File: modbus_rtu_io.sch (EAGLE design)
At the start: 60 parts, among them IC1 MAX3485ESA, IC5 ATMEGA48/88/168-PU, K1 AQY27SMD, K2 AQY22SOP, K3 G6D-1A-ASI12VDC, K4 RP418005, K5 AQG12105, K7 G6D-1A-ASI12VDC, K8 AQY22SOP, T1 BC846, T2 BC846, T4 BC846

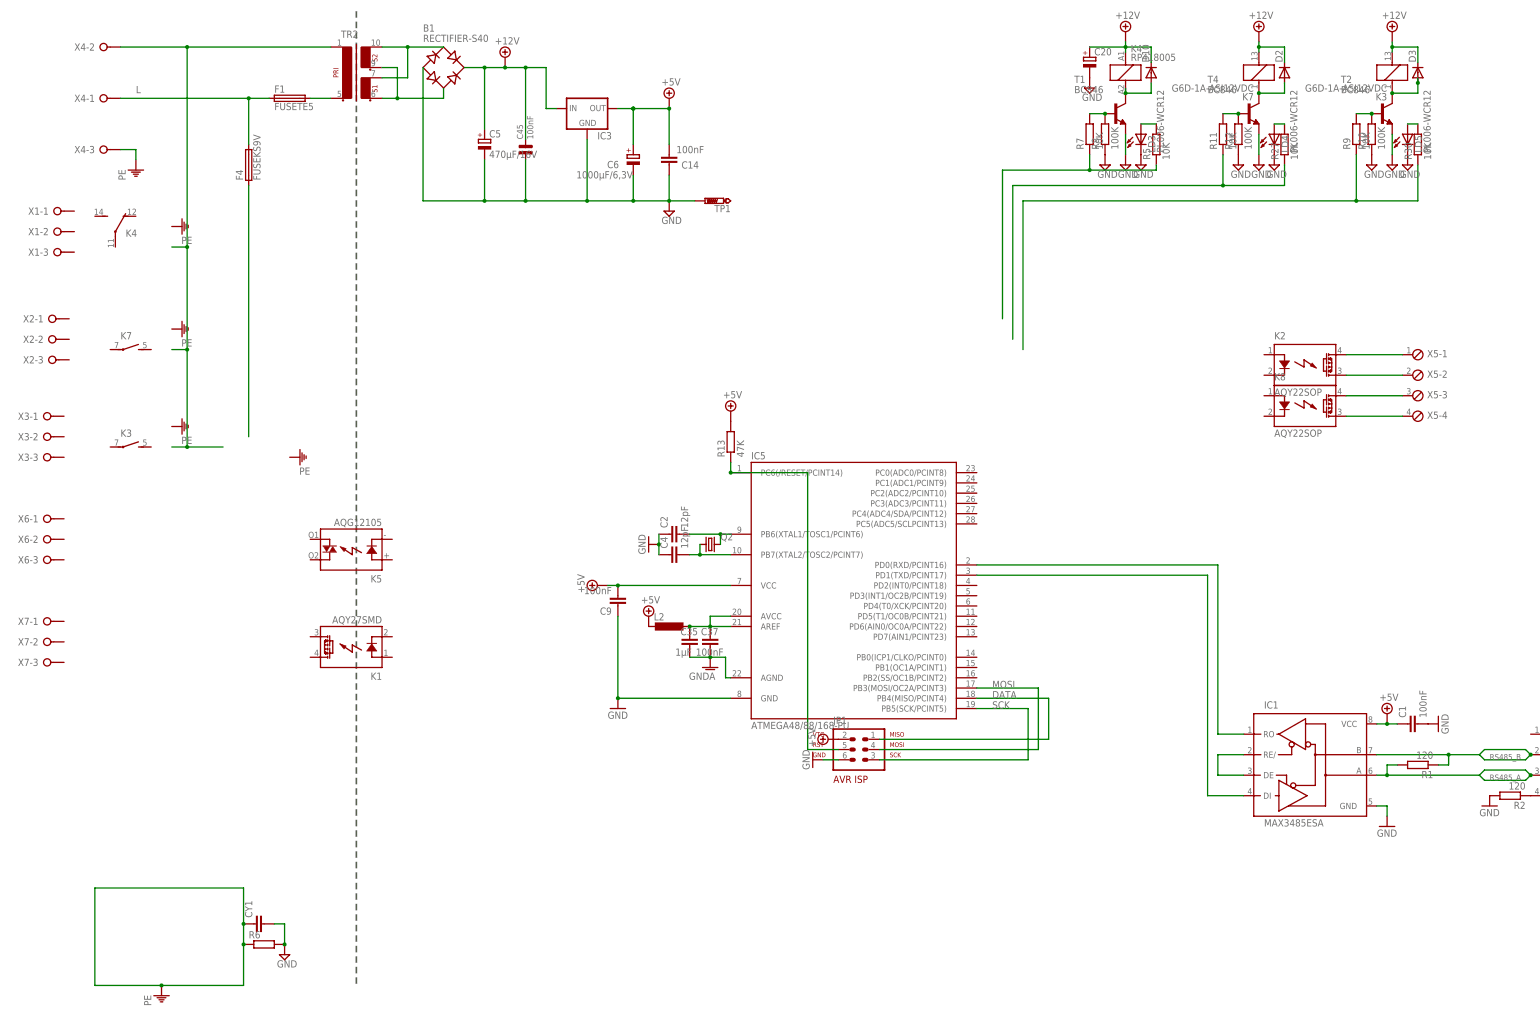
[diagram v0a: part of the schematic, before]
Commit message: Relais geändert, Routing angefangen
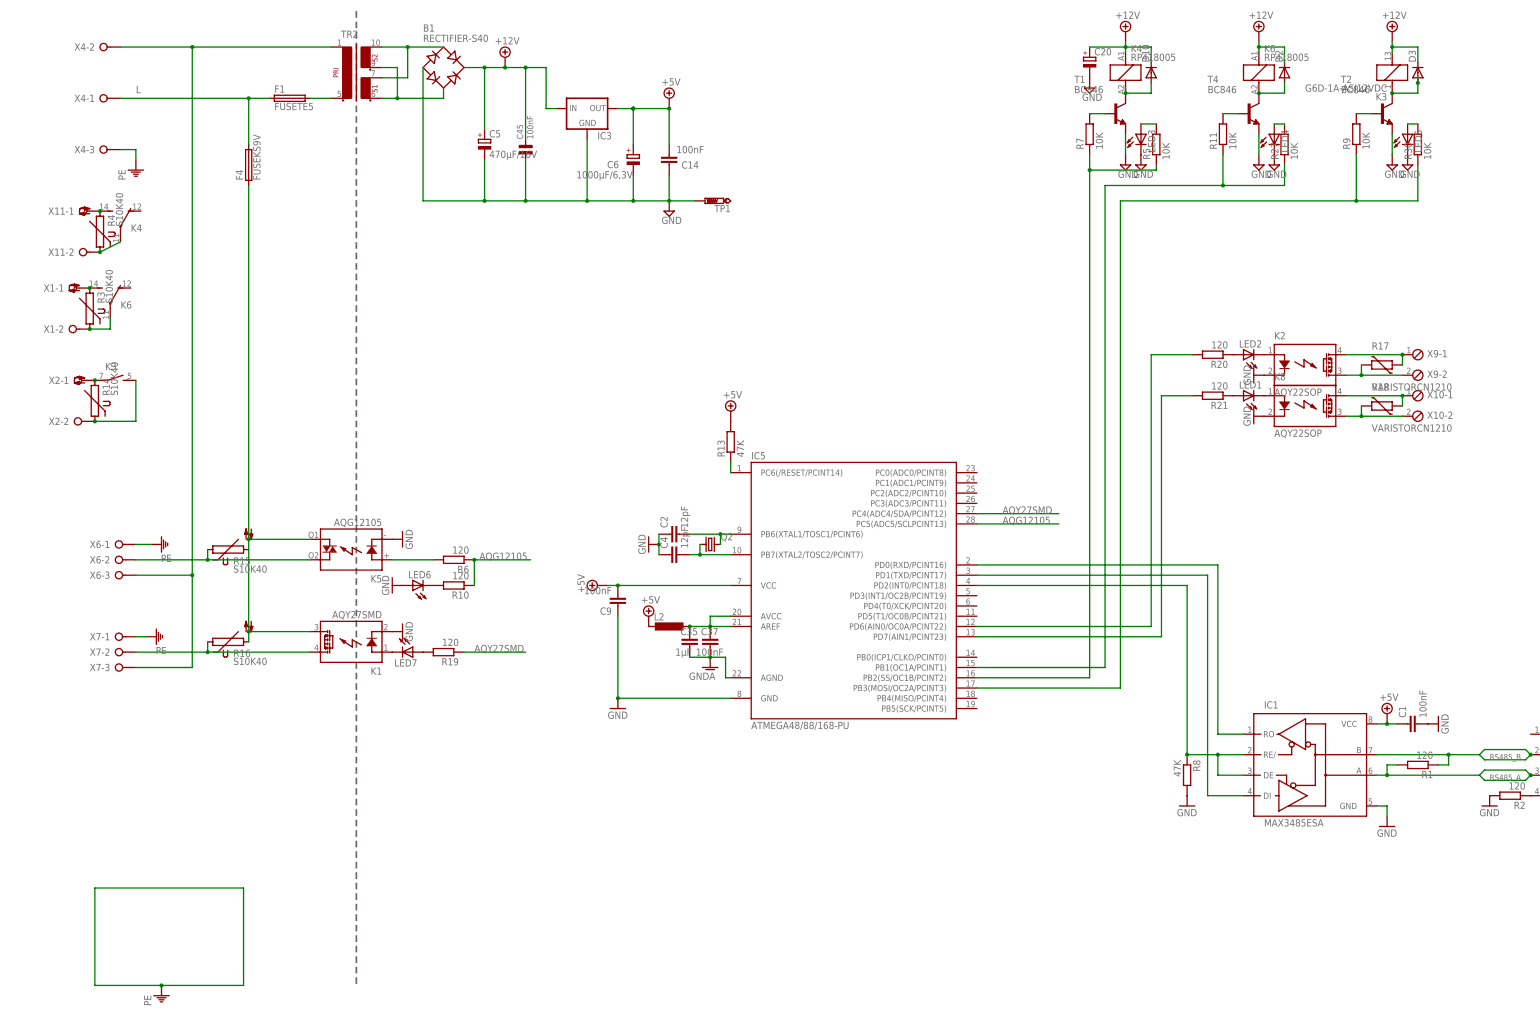
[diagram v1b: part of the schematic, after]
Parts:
- removed CY1: (no value), rcl:CYYC10B5
- removed JP1: AVR-ISP-6, atmel:AVR-ISP-6
- removed K7: G6D-1A-ASI12VDC, relay:G6D-1A-ASI12VDC
- removed LD3, LD4, LD5: PL006-WCR12, led:PL006-WCR12
- removed R12: 100K, rcl:R-EU_R0603
- removed X3: (no value), con-wago-508:W237-03P
- removed X5: (no value), con-phoenix-254:MPT4
- added K6: RP418005, relay:RP418005
- added LED1, LED2, LED3, LED4, LED5, LED6, LED7: (no value), led:LED3MM
- added R14, R15, R16, R3, R4: S10K40, varistor:S10K40
- added R17, R18: VARISTORCN1210, varistor:VARISTORCN1210
- added R19, R20, R21: 120, rcl:R-EU_R0603
- added X10, X9: (no value), con-phoenix-254:MPT2
- added X11: (no value), con-wago-508:W237-02P
- R10: value 100K -> 120
- R6: value (none) -> 120; device rcl:R-EU_0309/12 -> rcl:R-EU_R0603
- R8: value 100K -> 47K
- X1, X2: device con-wago-508:W237-03P -> con-wago-508:W237-02P
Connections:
- removed net DATA: IC5.PB4(MISO/PCINT4), JP1.1
- removed net MOSI: IC5.PB3(MOSI/OC2A/PCINT3), JP1.4
- removed net SCK: IC5.PB5(SCK/PCINT5), JP1.3
- new net AQG12105: IC5.PC5(ADC5/SCLPCINT13), R10.1, R6.1
- new net AQY27SMD: IC5.PC4(ADC4/SDA/PCINT12), R19.1
- new net N$24: K62.P, R3.1, X1-2.KL
- new net N$25: K32.P, R14.2, X2-1.KL
- new net N$26: K32.S, R14.1, X2-2.KL
- new net N$27: K5.DS1, R15.1, X6-2.KL
- new net N$29: K1.DS1, R16.1, X7-2.KL
- new net N$30: K5.A, R6.2
- new net N$31: K1.A, LED7.C
- new net N$32: K2.A, LED2.C
- new net N$35: K8.A, LED1.C
- new net N$37: IC5.PD6(AIN0/OC0A/PCINT22), R20.2
- new net N$38: IC5.PD7(AIN1/PCINT23), R21.2
- new net N$4: K42.P, R4.1, X11-2.KL
- new net N$41: LED1.A, R21.1
- new net N$42: LED2.A, R20.1
- new net N$43: LED7.A, R19.2
- new net N$44: LED6.C, R10.2
- new net N$5: K42.S, R4.2, X11-1.KL
- new net N$6: K62.S, R3.2, X1-1.KL
- net +12V: now also K61.1; no longer K71.2
- net +5V: no longer JP1.2
- net GND: now also K1.K, K2.K, K5.K, K8.K, LED3.C, LED4.C, LED5.C, LED6.A, R8.2; no longer CY1.2, JP1.6, LD3.C, LD4.C, LD5.C, R10.1, R12.1, R6.2, R8.1
- net N$13: no longer R12.2
- net N$14: now also K61.2; no longer K71.1
- net N$15: now also IC5.PD2(INT0/PCINT18), R8.1
- net N$16: now also R18.1, X10-1.1; no longer X5-3.1
- net N$18: now also R18.2, X10-2.1; no longer X5-4.1
- net N$2: no longer R10.2
- net N$20: now also R17.1, X9-1.1; no longer X5-1.1
- net N$21: now also R17.2, X9-2.1; no longer X5-2.1
- net N$28: now also X6-3.KL, X7-3.KL
- net N$3: now also LED3.A; no longer LD3.A
- net N$33: now also K1.DS2, K5.DS2, R15.2, R16.2
- net N$34: now also LED4.A; no longer LD4.A
- net N$36: now also IC5.PB2(SS/OC1B/PCINT2)
- net N$39: now also IC5.PB1(OC1A/PCINT1)
- net N$40: now also IC5.PB3(MOSI/OC2A/PCINT3)
- net N$50: now also LED5.A; no longer LD5.A
- net N$55: no longer JP1.5
- net N$7: no longer R8.2
- net PE: now also X6-1.KL, X7-1.KL; no longer CY1.1, R6.1
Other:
- moved on the sheet: K1, K3, K4, R10, R6, R8, X1-1, X1-2, X2-1, X2-2, X6-1, X6-2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

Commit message: routing fertig
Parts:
- removed X4: (no value), con-wago-508:W237-3N
- added C3, C7, C8: 100nF, rcl:C-EUC0603
- added LED8: (no value), led:LED3MM
- added R12, R23, R24: 120, rcl:R-EU_R0603
- added R22: 10K, rcl:R-EU_R0603
- added SL1: (no value), con-amp-quick:M03
- added SL2: (no value), con-amp-quick:M02
- added X3: GMSTBV3, con-phoenix-762:GMSTBV3
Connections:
- new net N$45: R12.1, X8-1.1
- new net N$51: LED8.C, R22.2
- new net N$53: C7.1, IC5.PD4(T0/XCK/PCINT20), R23.1, SL1.1
- new net N$56: C8.2, IC5.PC0(ADC0/PCINT8), R24.2, SL2.2
- net +12V: now also R12.2
- net +5V: now also C3.1, LED8.A, R23.2, SL1.3, SL2.1
- net GND: now also C3.2, C7.2, C8.1, R22.1, R24.1, SL1.2
- net L: now also X3-2.1; no longer X4-1.KL
- net N$23: now also TR2.1; no longer TR2.2
- net N$28: now also TR2.2, X3-3.1; no longer TR2.1, X4-2.KL
- net PE: now also X3-1.1; no longer X4-3.KL
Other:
- moved on the sheet: F1

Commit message: opto-mosfet package berichtigt, fertigung vorbereitet
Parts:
- removed K1: AQY27SMD, relay:AQY27SMD
- removed X10, X9: (no value), con-phoenix-254:MPT2
- added OK8: (no value), optocoupler:AQY280
- added SL3, SL4: (no value), con-amp-quick:M02
- added SL6: (no value), con-amp-quick:M04S
- added X4, X5: (no value), con-phoenix-254:MPT2
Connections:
- net GND: now also OK8.2; no longer K1.K
- net N$16: now also SL3.1; no longer X10-1.1
- net N$18: now also SL3.2; no longer X10-2.1
- net N$20: now also SL4.1; no longer X9-1.1
- net N$21: now also SL4.2; no longer X9-2.1
- net N$29: now also OK8.4; no longer K1.DS1
- net N$31: now also OK8.1; no longer K1.A
- net N$33: now also OK8.3; no longer K1.DS2
- net N$45: now also SL6-4.S; no longer X8-1.1
- net N$8: now also SL6-1.S; no longer X8-4.1
- net RS485_A: now also SL6-2.S; no longer X8-3.1
- net RS485_B: now also SL6-3.S; no longer X8-2.1
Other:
- moved on the sheet: C3, C7, LED7, R19, R23, X7-2, X8-1, X8-2, X8-3, X8-4
